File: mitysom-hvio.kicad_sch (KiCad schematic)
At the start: 28 parts, among them J1 Plug_Samtec_SEAM-50-02.0-L-08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, U1 TXS0102DQER, U48 TCA39306_VSSOP, U50 TCA39306_VSSOP

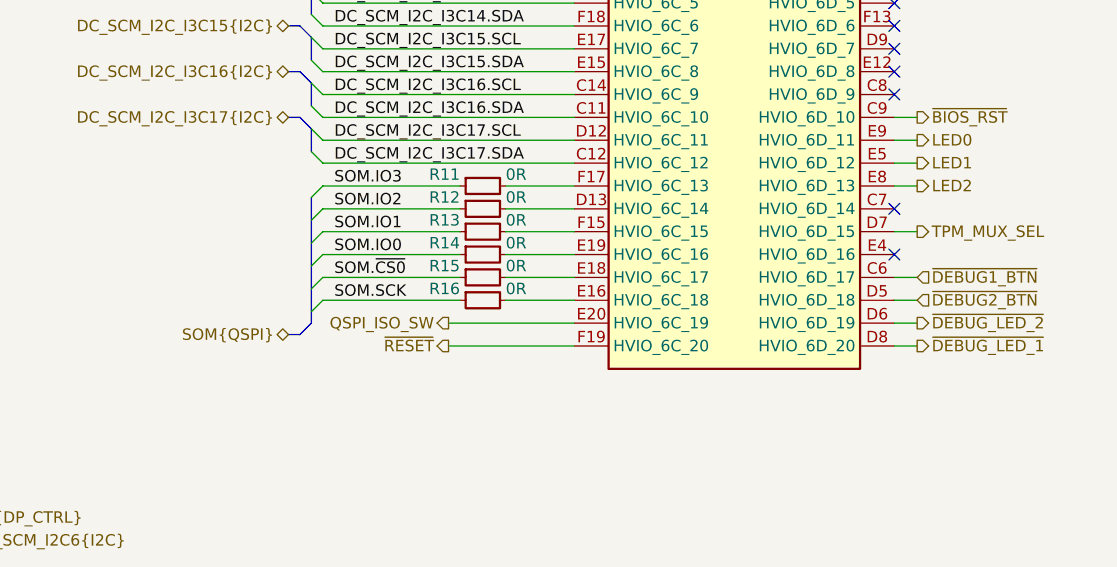
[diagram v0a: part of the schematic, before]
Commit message: [#100707] Connect QSPI CS1 to HVIO
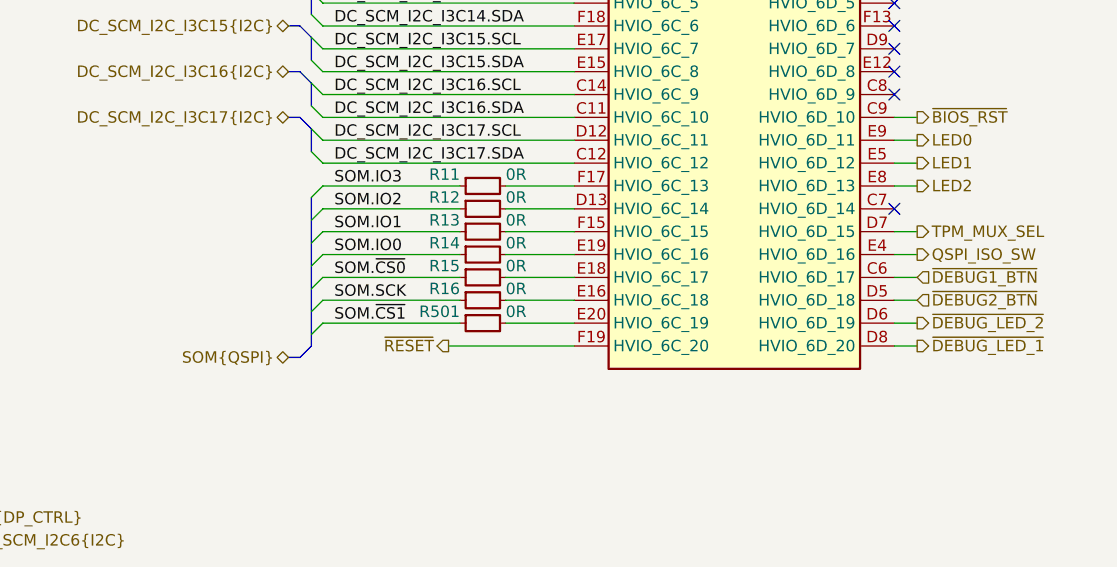
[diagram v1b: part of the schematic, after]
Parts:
- added R501: R_0R_0402, antmicro-footprints:R_0402_1005Metric, symbol antmicroResistors0402:R_0R_0402
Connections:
- net QSPI_ISO_SW: now also J1.E4 (HVIO_6D_16); no longer J1.E20 (HVIO_6C_19)
- new net: J1.E20 (HVIO_6C_19), R501.2
- new net SOM.~{CS1}: R501.1
- no-connect marks 13 -> 12
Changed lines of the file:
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@@
 	)
 	(no_connect
-		(at 302.26 179.07)
-	)
-	(no_connect
 		(at 302.26 173.99)
 	)
@@
 	)
 	(bus_entry
+		(at 238.76 186.69)
+		(size -1.27 1.27)
+		(stroke
+			(width 0)
+			(type default)
+		)
+	)
+	(bus_entry
 		(at 238.76 171.45)
 		(size -1.27 1.27)
@@
 		)
 	)
+	(bus
+		(pts
+			(xy 237.49 172.72) (xy 237.49 189.23)
+		)
+		(stroke
+			(width 0)
+			(type default)
+		)
+	)
 	(wire
 		(pts
@@
 	(bus
 		(pts
-			(xy 237.49 186.69) (xy 236.22 187.96)
+			(xy 237.49 189.23) (xy 236.22 190.5)
 		)
 		(stroke
@@
 	(bus
 		(pts
-			(xy 236.22 187.96) (xy 234.95 187.96)
+			(xy 236.22 190.5) (xy 234.95 190.5)
 		)
 		(stroke
@@
 	(wire
 		(pts
+			(xy 302.26 179.07) (xy 304.8 179.07)
+		)
+		(stroke
+			(width 0)
+			(type default)
+		)
+	)
+	(wire
+		(pts
 			(xy 139.7 124.46) (xy 139.7 123.19)
 		)
@@
 	(bus
 		(pts
-			(xy 237.49 186.69) (xy 237.49 172.72)
-		)
-		(stroke
-			(width 0)
-			(type default)
-		)
-	)
-	(bus
-		(pts
 			(xy 193.04 210.82) (xy 195.58 208.28)
 		)
@@
 	(wire
 		(pts
-			(xy 252.73 186.69) (xy 266.7 186.69)
+			(xy 259.08 186.69) (xy 266.7 186.69)
 		)
 		(stroke
@@
 	(wire
 		(pts
+			(xy 238.76 186.69) (xy 254 186.69)
+		)
+		(stroke
+			(width 0)
+			(type default)
+		)
+	)
+	(wire
+		(pts
 			(xy 69.85 139.7) (xy 73.66 139.7)
 		)
@@
 		)
 	)
+	(label "SOM.~{CS1}"
+		(at 240.03 186.69 0)
+		(effects
+			(font
+				(size 1.27 1.27)
+			)
+			(justify left bottom)
+		)
+	)
 	(label "DC_SCM_ESPI.~{CS0}"
 		(at 106.68 63.5 0)
@@
 		)
 	)
+	(hierarchical_label "QSPI_ISO_SW"
+		(shape output)
+		(at 304.8 179.07 0)
+		(effects
+			(font
+				(size 1.27 1.27)
+			)
+			(justify left)
+		)
+	)
 	(hierarchical_label "DC_SCM_I2C4{I2C}"
 		(shape bidirectional)
@@
 		)
 	)
-	(hierarchical_label "QSPI_ISO_SW"
-		(shape output)
-		(at 252.73 186.69 180)
-		(effects
-			(font
-				(size 1.27 1.27)
-			)
-			(justify right)
-		)
-	)
 	(hierarchical_label "SOM{QSPI}"
 		(shape bidirectional)
-		(at 234.95 187.96 180)
+		(at 234.95 190.5 180)
 		(effects
 			(font
@@
 		(polyline
 			(pts
-				(xy 262.89 185.42) (xy 265.43 185.42) (xy 265.43 170.18) (xy 262.89 170.18)
+				(xy 262.89 187.96) (xy 265.43 187.96) (xy 265.43 170.18) (xy 262.89 170.18)
 			)
 			(stroke
@@
 			(justify left bottom)
 		)
-		(property "Net Class" "50Ohm-se"
+		(property "Netclass" "50Ohm-se"
 			(at 100.33 63.5 0)
 			(show_name no)
@@
 			(justify right bottom)
 		)
-		(property "Net Class" "50Ohm-se"
+		(property "Netclass" "50Ohm-se"
 			(at 201.93 60.96 0)
 			(show_name no)
@@
 			(justify right bottom)
 		)
-		(property "Net Class" "90Ohm-diff"
+		(property "Netclass" "90Ohm-diff"
 			(at 199.39 226.06 0)
 			(show_name no)
@@
 		(length 2.54)
 		(shape round)
-		(at 265.43 185.42 180)
+		(at 265.43 187.96 180)
 		(fields_autoplaced yes)
 		(effects
@@
 			(justify right bottom)
 		)
-		(property "Net Class" "50Ohm-se"
-			(at 264.7315 187.96 0)
+		(property "Netclass" "50Ohm-se"
+			(at 264.7315 190.5 0)
 			(show_name no)
 			(do_not_autoplace no)
@@
 		)
 		(property "Component Class" ""
-			(at 118.11 15.24 0)
+			(at 118.11 17.78 0)
 			(show_name no)
 			(do_not_autoplace no)
@@
 					(unit 1)
 				)
+			)
+		)
+	)
+	(symbol
+		(lib_id "antmicroResistors0402:R_0R_0402")
+		(at 254 186.69 0)
+		(unit 1)
+		(body_style 1)
+		(exclude_from_sim no)
+		(in_bom yes)
+		(on_board yes)
+		(in_pos_files yes)
+		(dnp no)
+		(property "Reference" "R501"
+			(at 254 185.42 0)
+			(show_name no)
+			(do_not_autoplace no)
+			(effects
+				(font
+					(size 1.27 1.27)
+					(thickness 0.15)
+				)
+				(justify right)
+			)
+		)
+		(property "Value" "R_0R_0402"
+			(at 274.32 199.39 0)
+			(hide yes)
+			(show_name no)
+			(do_not_autoplace no)
+			(effects
+				(font
+					(size 1.27 1.27)
+					(thickness 0.15)
+				)
+				(justify left bottom)
+			)
+		)
+		(property "Footprint" "antmicro-footprints:R_0402_1005Metric"
+			(at 274.32 201.93 0)
+			(hide yes)
+			(show_name no)
+			(do_not_autoplace no)
+			(effects
+				(font
+					(size 1.27 1.27)
+					(thickness 0.15)
+				)
+				(justify left bottom)
+			)
+		)
+		(property "Datasheet" "https://industrial.panasonic.com/cdbs/www-data/pdf/RDA0000/AOA0000C301.pdf"
+			(at 274.32 204.47 0)
+			(hide yes)
+			(show_name no)
+			(do_not_autoplace no)
+			(effects
+				(font
+					(size 1.27 1.27)
+					(thickness 0.15)
+				)
+				(justify left bottom)
+			)
+		)
+		(property "Description" "SMD Chip Resistor, Jumper, 0 ohm, 100 mW, 0402 [1005 Metric], Thick Film, General Purpose"
+			(at 254 186.69 0)
+			(hide yes)
+			(show_name no)
+			(do_not_autoplace no)
+			(effects
+				(font
+					(size 1.27 1.27)
+				)
+			)
+		)
+		(property "MPN" "ERJ2GE0R00X"
+			(at 274.32 207.01 0)
+			(hide yes)
+			(show_name no)
+			(do_not_autoplace no)
+			(effects
+				(font
+					(size 1.27 1.27)
+					(thickness 0.15)
+				)
+				(justify left bottom)
+			)
+		)
+		(property "Manufacturer" "Panasonic"
+			(at 274.32 209.55 0)
+			(hide yes)
+			(show_name no)
+			(do_not_autoplace no)
+			(effects
+				(font
+					(size 1.27 1.27)
+					(thickness 0.15)
+				)
+				(justify left bottom)
+			)
+		)
+		(property "License" "Apache-2.0"
+			(at 274.32 212.09 0)
+			(hide yes)
+			(show_name no)
+			(do_not_autoplace no)
+			(effects
+				(font
+					(size 1.27 1.27)
+					(thickness 0.15)
+				)
+				(justify left bottom)
+			)
+		)
+		(property "Author" "Antmicro"
+			(at 274.32 214.63 0)
+			(hide yes)
+			(show_name no)
+			(do_not_autoplace no)
+			(effects
+				(font
+					(size 1.27 1.27)
+					(thickness 0.15)
+				)
+				(justify left bottom)
+			)
+		)
+		(property "Val" "0R"
+			(at 259.08 185.42 0)
+			(show_name no)
+			(do_not_autoplace no)
+			(effects
+				(font
+					(size 1.27 1.27)
+					(thickness 0.15)
+				)
+				(justify left)
+			)
+		)
+		(property "Tolerance" ""
+			(at 274.32 196.85 0)
+			(hide yes)
+			(show_name no)
+			(do_not_autoplace no)
+			(effects
+				(font
+					(size 1.27 1.27)
+				)
+				(justify left bottom)
+			)
+		)
+		(property "Current" "1A"
+			(at 274.32 217.17 0)
+			(hide yes)
+			(show_name no)
+			(do_not_autoplace no)
+			(effects
+				(font
+					(size 1.27 1.27)
+					(thickness 0.15)
+				)
+				(justify left bottom)
+			)
+		)
+		(pin "1"
+		)
+		(pin "2"
+		)
+		(instances
+			(project "altera-modular-agilex-5-dc-scm"
+				(path "/6bb9d978-a328-4b30-874b-55170a976185/c1ff3762-7815-4072-9586-bdd6f23ff1ef"
+					(reference "R501")
+					(unit 1)
+				)

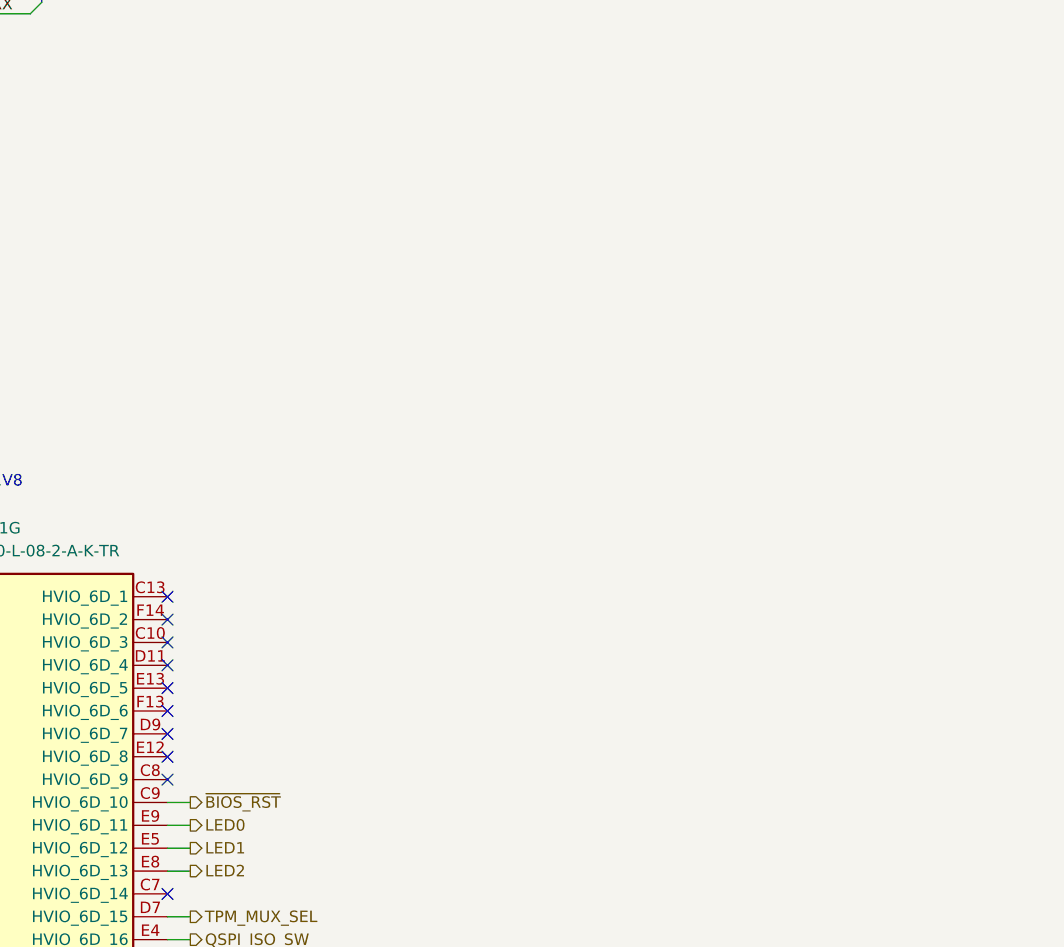
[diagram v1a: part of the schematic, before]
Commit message: [#101136] Connect DC-SCM JTAG to HVIO. Expose HPS JTAG on debug connector
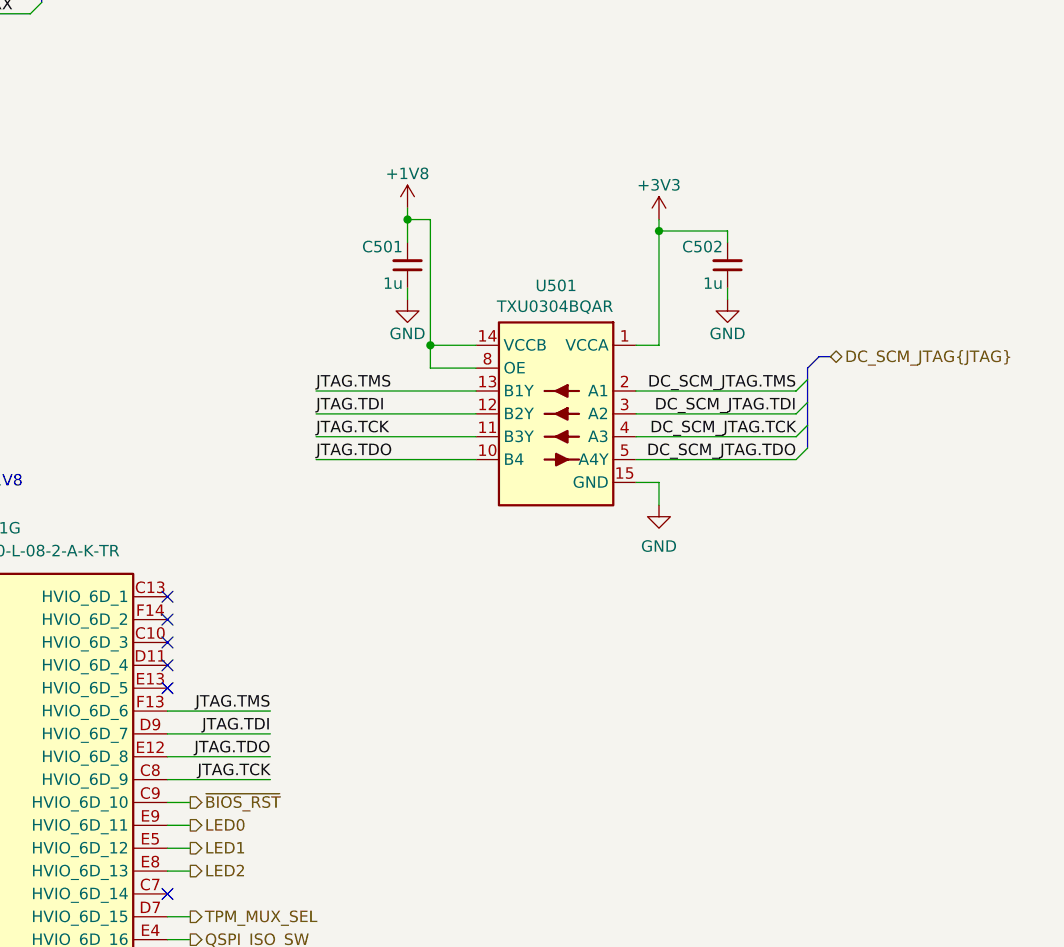
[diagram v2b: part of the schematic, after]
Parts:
- added C501, C502: C_1u_25V_0402, antmicro-footprints:C_0402_1005Metric, symbol antmicroCapacitors0402:C_1u_25V_0402
- added U501: TXU0304BQAR, antmicro-footprints:DHVQFN-14-1EP_2.5x3mm, symbol antmicroLogicTranslatorsLevelShifters:TXU0304BQAR
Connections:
- net +1V8: now also C501.2, U501.14 (VCCB), U501.8 (OE)
- net +3V3: now also C502.2, U501.1 (VCCA)
- net GND: now also C501.1, C502.1, U501.15 (GND), U501.7 (GND)
- net JTAG.TCK: now reaches J1.C8 (HVIO_6D_9)
- net JTAG.TCK: now also U501.11 (B3Y)
- net JTAG.TDI: now reaches J1.D9 (HVIO_6D_7)
- net JTAG.TDI: now also U501.12 (B2Y)
- net JTAG.TDO: now reaches J1.E12 (HVIO_6D_8)
- net JTAG.TDO: now also U501.10 (B4)
- net JTAG.TMS: now reaches J1.F13 (HVIO_6D_6)
- net JTAG.TMS: now also U501.13 (B1Y)
- new net DC_SCM_JTAG.TCK: U501.4 (A3)
- new net DC_SCM_JTAG.TDI: U501.3 (A2)
- new net DC_SCM_JTAG.TDO: U501.5 (A4Y)
- new net DC_SCM_JTAG.TMS: U501.2 (A1)
- no-connect marks 12 -> 8

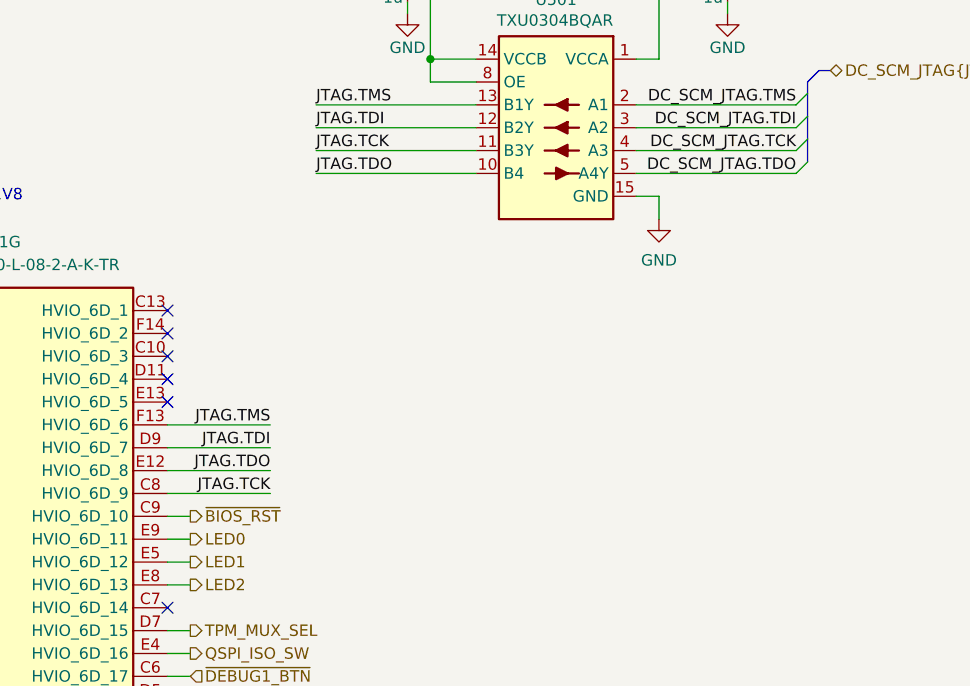
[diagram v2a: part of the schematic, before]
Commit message: [#101136] Connect DC-SCM JTAG TRST to HVIO
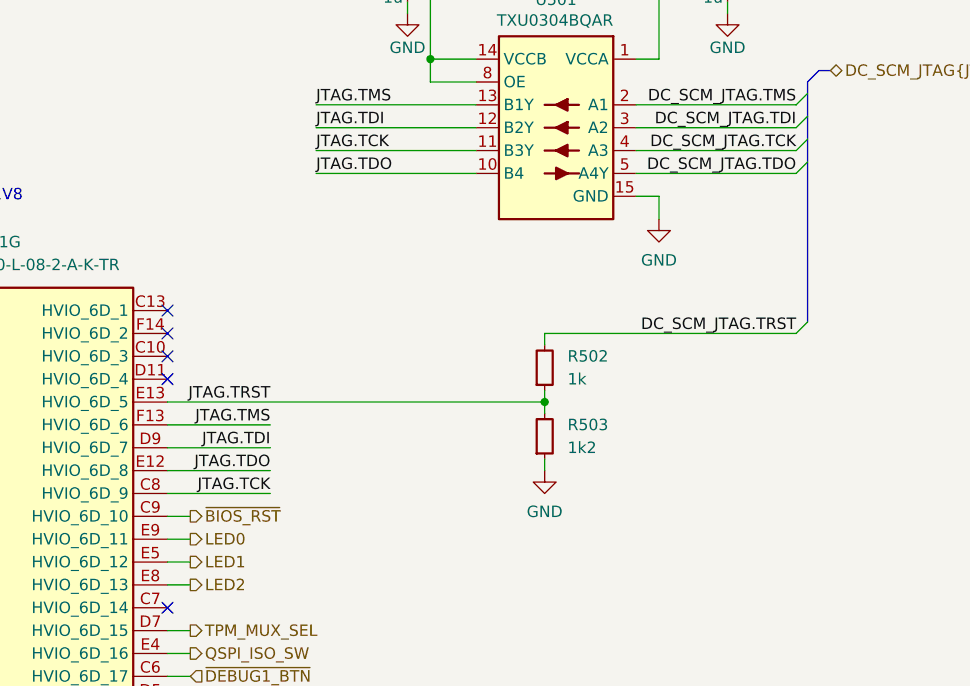
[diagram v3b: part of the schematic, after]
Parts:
- added R502: R_1k_0402, antmicro-footprints:R_0402_1005Metric, symbol antmicroResistors0402:R_1k_0402
- added R503: R_1k2_0402, antmicro-footprints:R_0402_1005Metric, symbol antmicroResistors0402:R_1k2_0402
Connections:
- net GND: now also R503.1
- net JTAG.TRST: now reaches J1.E13 (HVIO_6D_5)
- net JTAG.TRST: now also R502.1, R503.2
- new net DC_SCM_JTAG.TRST: R502.2
- no-connect marks 8 -> 7
